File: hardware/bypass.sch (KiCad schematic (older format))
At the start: 10 parts, among them Q1 BSS138

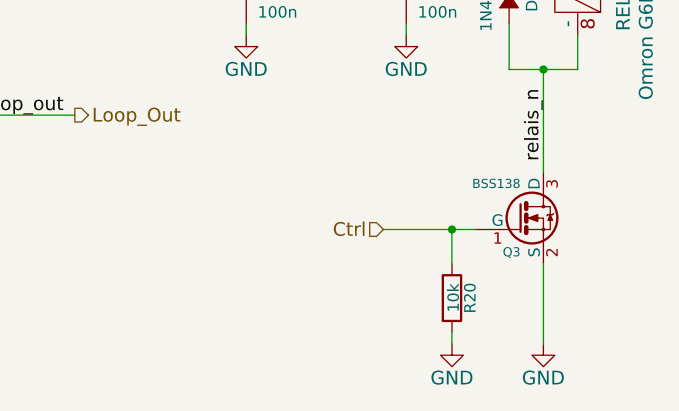
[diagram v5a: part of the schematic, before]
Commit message: Initial placement and bom optimization
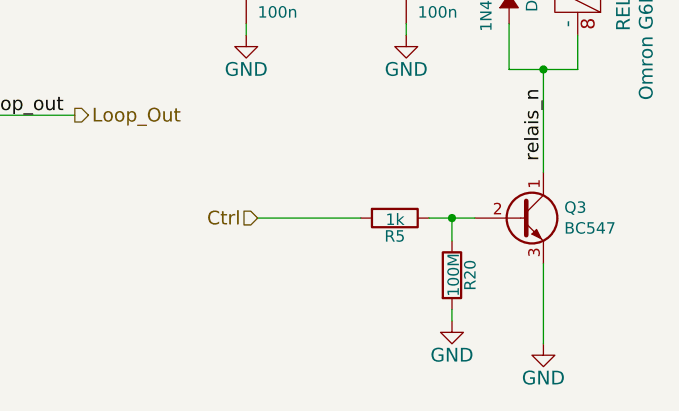
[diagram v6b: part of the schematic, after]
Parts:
- removed Q1: BSS138, Package_TO_SOT_SMD:SOT-23_Handsoldering, symbol uMIDI-wah-rescue:BSS138-uMIDI-switcher-rescue
- added Q3: BC547, Package_TO_SOT_THT:TO-92_Inline, symbol Transistor_BJT:BC547
- added R5: 1k, Resistor_SMD:R_0805_2012Metric_Pad1.15x1.40mm_HandSolder, symbol uMIDI-wah-rescue:R-uMIDI-switcher-rescue
- R6: value 10k -> 100M
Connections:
- net Ctrl: now also R5.2; no longer R6.1
- net GND: now also Q3.3 (E)
- net relais_n: now also Q3.1 (C)
- new net: Q3.2 (B), R5.1, R6.1
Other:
- moved on the sheet: R20
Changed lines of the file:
@@
 Text HLabel 4700 3150 1    60   Input ~ 0
 FX_Return
-Text HLabel 7200 4300 0    60   Input ~ 0
+Text HLabel 6650 4250 0    60   Input ~ 0
 Ctrl
 $Comp
@@
 L uMIDI-wah-rescue:R-uMIDI-switcher-rescue R6
 U 1 1 54D7ADF3
-P 7500 4600
+P 7500 4500
 AR Path="/56223A3E/54D7ADF3" Ref="R6"  Part="1"
 AR Path="/56223A52/54E9BE9F/54D7ADF3" Ref="R11"  Part="1"
@@
 AR Path="/56223A90/54E9BE9F/54D7ADF3" Ref="R31"  Part="1"
 AR Path="/5CD91DFE/54D7ADF3" Ref="R20"  Part="1"
-F 0 "R20" V 7580 4600 50  0000 C CNN
-F 1 "10k" V 7507 4601 50  0000 C CNN
-F 2 "Resistor_SMD:R_0805_2012Metric_Pad1.15x1.40mm_HandSolder" V 7430 4600 30  0001 C CNN
-F 3 "" H 7580 4600 60  0001 C CNN
-F 4 "Mouser" H 7580 4600 60  0001 C CNN "Supplier"
-F 5 "71-CRCW0603J-10K-E3" H 7580 4600 60  0001 C CNN "Supplier Part Number"
-F 6 "http://eu.mouser.com/ProductDetail/Vishay-Dale/CRCW060310K0JNEA/?qs=sGAEpiMZZMu61qfTUdNhG%2fEx4adfNLScijTXbM5aXyk%3d" H 7580 4600 60  0001 C CNN "Supplier Link"
-F 7 "Vishay/Dale" H 7580 4600 60  0001 C CNN "Manufacturer"
-F 8 "CRCW060310K0JNEA" H 7580 4600 60  0001 C CNN "Manufacturer Part Number"
-F 9 "http://www.vishay.com/resistors-fixed/list/product-20011/" H 7580 4600 60  0001 C CNN "Manufacturer Link"
-	1    7500 4600
-	1    0    0    -1
-$EndComp
-$Comp
-L uMIDI-wah-rescue:BSS138-uMIDI-switcher-rescue Q1
-U 1 1 54D7AECB
-P 7800 4250
-AR Path="/56223A3E/54D7AECB" Ref="Q1"  Part="1"
-AR Path="/56223A52/54E9BE9F/54D7AECB" Ref="Q2"  Part="1"
-AR Path="/56223A60/54E9BE9F/54D7AECB" Ref="Q3"  Part="1"
-AR Path="/56223A6E/54E9BE9F/54D7AECB" Ref="Q4"  Part="1"
-AR Path="/56223A7C/54E9BE9F/54D7AECB" Ref="Q5"  Part="1"
-AR Path="/56223A90/54E9BE9F/54D7AECB" Ref="Q6"  Part="1"
-AR Path="/54D7AECB" Ref="Q1"  Part="1"
-AR Path="/5CD91DFE/54D7AECB" Ref="Q3"  Part="1"
-F 0 "Q3" H 7800 4101 40  0000 R CNN
-F 1 "BSS138" H 7800 4400 40  0000 R CNN
-F 2 "Package_TO_SOT_SMD:SOT-23_Handsoldering" H 7670 4352 29  0001 C CNN
-F 3 "https://www.fairchildsemi.com/datasheets/BS/BSS138.pdf" H 7800 4101 60  0001 C CNN
-F 4 "Mouser" H 3650 5050 60  0001 C CNN "Supplier"
-F 5 "512-BSS138 " H 3650 5050 60  0001 C CNN "Supplier Part Number"
-F 6 "http://eu.mouser.com/ProductDetail/Fairchild-Semiconductor/BSS138/?qs=sGAEpiMZZMshyDBzk1%2fWi1qxDdW%2fXBi2IwQV99jpxW8%3d" H 3650 5050 60  0001 C CNN "Supplier Link"
-F 7 "Fairchild" H 3650 5050 60  0001 C CNN "Manufacturer"
-F 8 "BSS138" H 3650 5050 60  0001 C CNN "Manufacturer Part Number"
-	1    7800 4250
+F 0 "R20" V 7580 4500 50  0000 C CNN
+F 1 "100M" V 7507 4501 50  0000 C CNN
+F 2 "Resistor_SMD:R_0805_2012Metric_Pad1.15x1.40mm_HandSolder" V 7430 4500 30  0001 C CNN
+F 3 "" H 7580 4500 60  0001 C CNN
+F 4 "Mouser" H 7580 4500 60  0001 C CNN "Supplier"
+F 5 "71-CRCW0603J-10K-E3" H 7580 4500 60  0001 C CNN "Supplier Part Number"
+F 6 "http://eu.mouser.com/ProductDetail/Vishay-Dale/CRCW060310K0JNEA/?qs=sGAEpiMZZMu61qfTUdNhG%2fEx4adfNLScijTXbM5aXyk%3d" H 7580 4500 60  0001 C CNN "Supplier Link"
+F 7 "Vishay/Dale" H 7580 4500 60  0001 C CNN "Manufacturer"
+F 8 "CRCW060310K0JNEA" H 7580 4500 60  0001 C CNN "Manufacturer Part Number"
+F 9 "http://www.vishay.com/resistors-fixed/list/product-20011/" H 7580 4500 60  0001 C CNN "Manufacturer Link"
+	1    7500 4500
 	1    0    0    -1
 $EndComp
@@
 L power:GND #PWR039
 U 1 1 54D7B0C5
-P 7500 4800
+P 7500 4700
 AR Path="/56223A3E/54D7B0C5" Ref="#PWR039"  Part="1"
 AR Path="/56223A52/54E9BE9F/54D7B0C5" Ref="#PWR046"  Part="1"
@@
 AR Path="/56223A90/54E9BE9F/54D7B0C5" Ref="#PWR074"  Part="1"
 AR Path="/5CD91DFE/54D7B0C5" Ref="#PWR023"  Part="1"
-F 0 "#PWR023" H 7500 4550 60  0001 C CNN
-F 1 "GND" H 7500 4650 60  0000 C CNN
-F 2 "" H 7500 4800 60  0000 C CNN
-F 3 "" H 7500 4800 60  0000 C CNN
-	1    7500 4800
-	1    0    0    -1
-$EndComp
-Wire Wire Line
-	7200 4300 7500 4300
-Wire Wire Line
-	7500 4300 7500 4450
-Connection ~ 7500 4300
+F 0 "#PWR023" H 7500 4450 60  0001 C CNN
+F 1 "GND" H 7500 4550 60  0000 C CNN
+F 2 "" H 7500 4700 60  0000 C CNN
+F 3 "" H 7500 4700 60  0000 C CNN
+	1    7500 4700
+	1    0    0    -1
+$EndComp
 $Comp
 L uMIDI-wah-rescue:R-uMIDI-switcher-rescue R5
@@
 	7300 3450 7300 3400
 Wire Wire Line
-	7500 4800 7500 4750
+	7500 4700 7500 4650
 Text Label 4300 3900 0    60   ~ 0
 bypass
@@
 	6600 3000 6800 3000
 Wire Wire Line
-	7500 4300 7600 4300
-Wire Wire Line
 	7300 3000 7750 3000
+$Comp
+L Transistor_BJT:BC547 Q?
+U 1 1 5CE6B092
+P 7800 4250
+AR Path="/5C8EC687/5CE6B092" Ref="Q?"  Part="1"
+AR Path="/5C8EFAFF/5CE6B092" Ref="Q?"  Part="1"
+AR Path="/5CD91DFE/5CE6B092" Ref="Q3"  Part="1"
+F 0 "Q3" H 7991 4296 50  0000 L CNN
+F 1 "BC547" H 7991 4205 50  0000 L CNN
+F 2 "Package_TO_SOT_THT:TO-92_Inline" H 8000 4175 50  0001 L CIN
+F 3 "http://www.fairchildsemi.com/ds/BC/BC547.pdf" H 7800 4250 50  0001 L CNN
+	1    7800 4250
+	1    0    0    -1
+$EndComp
+$Comp
+L uMIDI-wah-rescue:R-uMIDI-switcher-rescue R?
+U 1 1 5CE6C2B1
+P 7250 4250
+AR Path="/56223A3E/5CE6C2B1" Ref="R?"  Part="1"
+AR Path="/56223A52/54E9BE9F/5CE6C2B1" Ref="R?"  Part="1"
+AR Path="/56223A60/54E9BE9F/5CE6C2B1" Ref="R?"  Part="1"
+AR Path="/56223A6E/54E9BE9F/5CE6C2B1" Ref="R?"  Part="1"
+AR Path="/56223A7C/54E9BE9F/5CE6C2B1" Ref="R?"  Part="1"
+AR Path="/56223A90/54E9BE9F/5CE6C2B1" Ref="R?"  Part="1"
+AR Path="/5CD91DFE/5CE6C2B1" Ref="R5"  Part="1"
+F 0 "R5" V 7330 4250 50  0000 C CNN
+F 1 "1k" V 7257 4251 50  0000 C CNN
+F 2 "Resistor_SMD:R_0805_2012Metric_Pad1.15x1.40mm_HandSolder" V 7180 4250 30  0001 C CNN
+F 3 "" H 7330 4250 60  0001 C CNN
+F 4 "" H 7330 4250 60  0001 C CNN "Supplier"
+F 5 "" H 7330 4250 60  0001 C CNN "Supplier Part Number"
+F 6 "" H 7330 4250 60  0001 C CNN "Supplier Link"
+F 7 "" H 7330 4250 60  0001 C CNN "Manufacturer"
+F 8 "" H 7330 4250 60  0001 C CNN "Manufacturer Part Number"
+F 9 "" H 7330 4250 60  0001 C CNN "Manufacturer Link"
+	1    7250 4250
+	0    1    1    0
+$EndComp
+Wire Wire Line
+	7400 4250 7500 4250
+Wire Wire Line
+	7500 4350 7500 4250
+Connection ~ 7500 4250
+Wire Wire Line
+	7500 4250 7600 4250
+Wire Wire Line
+	6650 4250 7100 4250
 $EndSCHEMATC

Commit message: Add missing manufacturer links
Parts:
- C13: Supplier (none) -> RS; Supplier Link (none) -> https://de.rs-online.com/web/p/keramik-vielschichtkondensat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; Supplier Part Number (none) -> 170-0041
- C14: Manufacturer Murata -> (none); Manufacturer Part Number GRM188R71E104KA01D -> (none); Supplier Mouser -> RS; Supplier Link http://eu.mouser.com/ProductDetail/Murata-Electronics/GRM18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 -> https://de.rs-online.com/web/p/keramik-vielschichtkondensat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; Supplier Part Number 81-GRM39X104K25 -> 170-0041
- D2: Manufacturer Diodes Incorporated -> Diodes Zetex; Supplier Mouser -> RS; Supplier Link http://eu.mouser.com/ProductDetail/Diodes-Incorporated/1N41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 -> https://de.rs-online.com/web/p/schaltdioden/7384728/; Supplier Part Number 621-1N4148W-F -> 738-4728
- Q3: Supplier (none) -> RS; Supplier Link (none) -> https://de.rs-online.com/web/p/bipolare-transistoren/166298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; Supplier Part Number (none) -> 166-2988
- R2: Supplier (none) -> RS; Supplier Link (none) -> https://de.rs-online.com/web/p/smd-widerstande/2945062/; Supplier Part Number (none) -> 294-5062
- R3, R4: Manufacturer Vishay/Dale -> (none); Manufacturer Part Number CRCW0603100MJPEAHR -> (none); Supplier Mouser -> RS; Supplier Link http://eu.mouser.com/ProductDetail/Vishay-Dale/CRCW0603100M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 -> https://de.rs-online.com/web/p/smd-widerstande/2945062/; Supplier Part Number 71-CRCW0603100MJPEA -> 294-5062
- R5: Manufacturer Part Number CRCW0603180RJNEA -> CRCW0805180RFKEA; Supplier Mouser -> RS; Supplier Link http://www.mouser.de/ProductDetail/Vishay-Dale/CRCW0603180R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 -> https://de.rs-online.com/web/p/smd-widerstande/6790942/; Supplier Part Number 71-CRCW0603J-180-E3 -> 679-0942
- R5: Supplier (none) -> RS; Supplier Link (none) -> https://de.rs-online.com/web/p/smd-widerstande/8046449/; Supplier Part Number (none) -> 804-6449
- R6: Manufacturer Vishay/Dale -> (none); Manufacturer Part Number CRCW060310K0JNEA -> (none); Supplier Mouser -> RS; Supplier Link http://eu.mouser.com/ProductDetail/Vishay-Dale/CRCW060310K0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 -> https://de.rs-online.com/web/p/smd-widerstande/2945062/; Supplier Part Number 71-CRCW0603J-10K-E3 -> 294-5062
- REL1: Manufacturer Part Number G6K-2P-Y-DC5 -> G6K-2P-Y 5DC; Supplier Mouser -> RS; Supplier Link http://eu.mouser.com/ProductDetail/Omron-Electronics/G6K-2P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 -> https://de.rs-online.com/web/p/monostabile-relais/3650440/; Supplier Part Number 653-G6K-2P-Y-DC5 -> 365-0440
